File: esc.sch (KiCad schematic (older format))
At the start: 67 parts, among them IC1 4N25, IC2 LM25101, IC3 LM25101, IC4 LM25101, IC5 ATMEGA8-AI, P1 CONN_01X03, P2 CONN_01X03, P3 CONN_01X02, P4 CONN_02X02, P5 CONN_01X01, P6 CONN_01X01, Q1 MOSFET_N, Q10 MOSFET_N, Q11 MOSFET_N, Q12 MOSFET_N, Q2 MOSFET_N, Q3 MOSFET_N, Q4 MOSFET_N, Q5 MOSFET_N, Q6 MOSFET_N, Q7 MOSFET_N, Q8 MOSFET_N, Q9 MOSFET_N, U1 MCP1804, U2 LM2940 10V, Y1 RESONATEUR

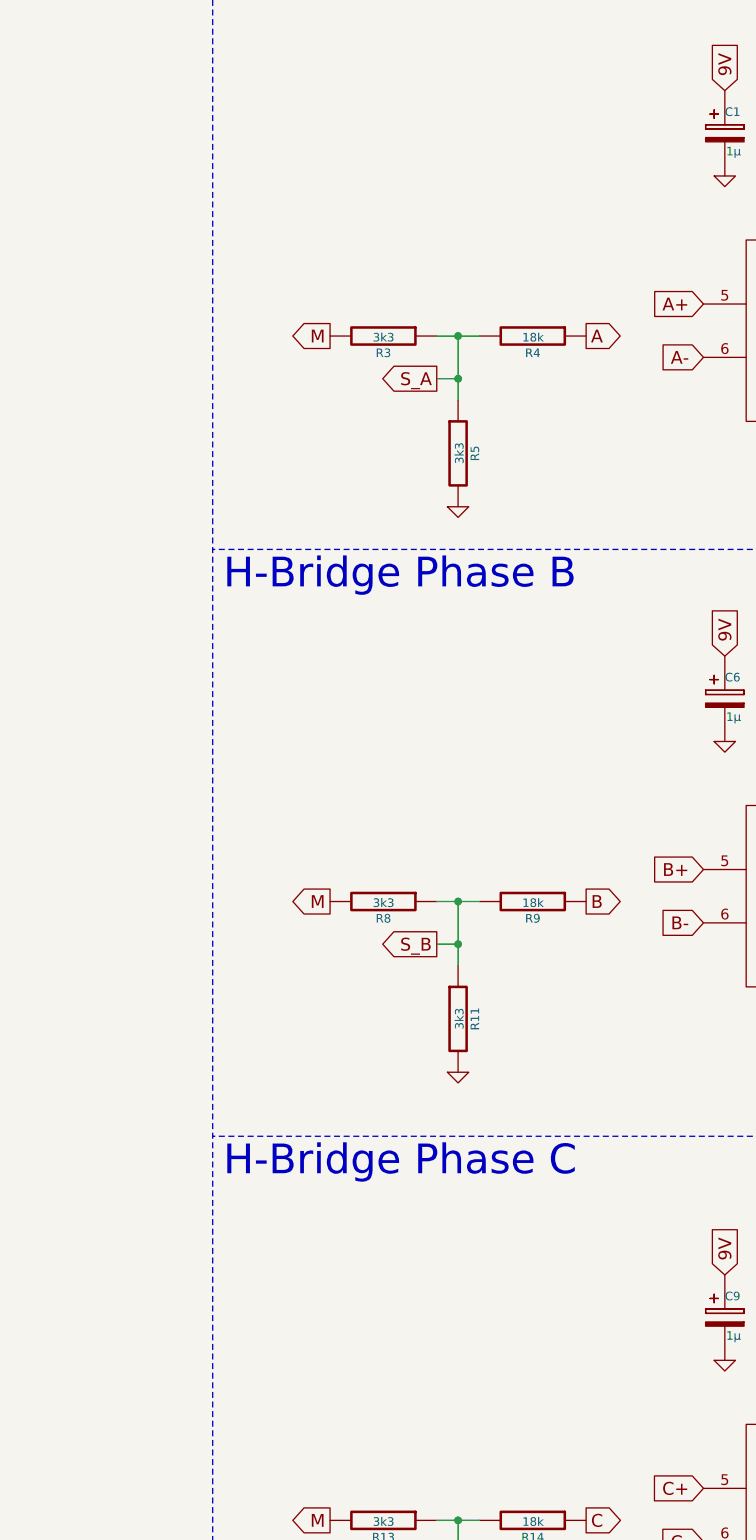
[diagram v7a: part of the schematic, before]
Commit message: Added pull down Resistors
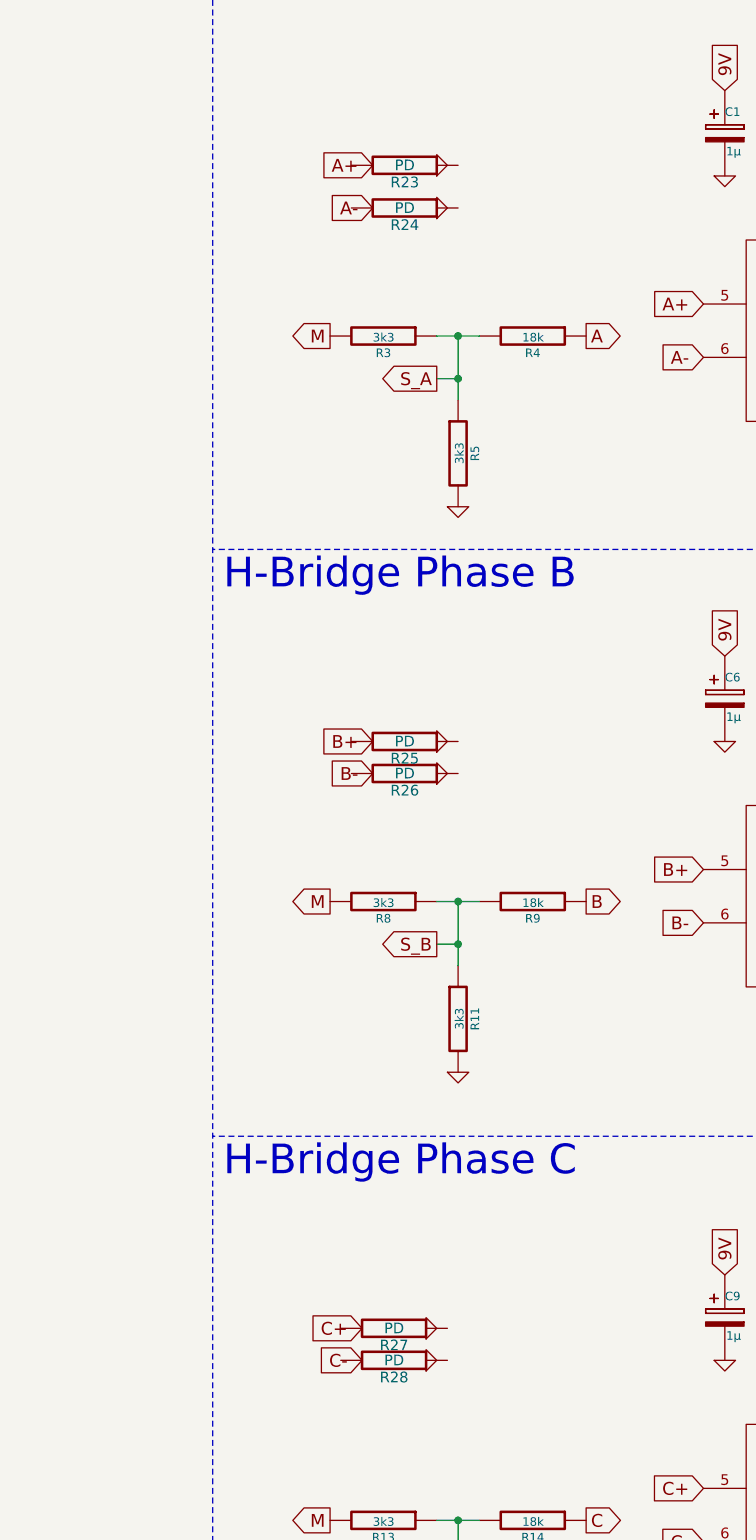
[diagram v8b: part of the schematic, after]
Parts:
- added R23, R24, R25, R26, R27, R28: PD, Resistors_SMD:R_0603_HandSoldering, symbol R
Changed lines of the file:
@@
 	1    0    0    -1
 $EndComp
+Text GLabel 9900 7350 0    60   Input ~ 0
+C+
+Text GLabel 9900 7500 0    60   Input ~ 0
+C-
+$Comp
+L R R27
+U 1 1 564C95B9
+P 10050 7350
+F 0 "R27" V 10130 7350 50  0000 C CNN
+F 1 "PD" V 10050 7350 50  0000 C CNN
+F 2 "Resistors_SMD:R_0603_HandSoldering" V 9980 7350 30  0001 C CNN
+F 3 "" H 10050 7350 30  0000 C CNN
+	1    10050 7350
+	0    1    1    0
+$EndComp
+$Comp
+L R R28
+U 1 1 564C9864
+P 10050 7500
+F 0 "R28" V 10130 7500 50  0000 C CNN
+F 1 "PD" V 10050 7500 50  0000 C CNN
+F 2 "Resistors_SMD:R_0603_HandSoldering" V 9980 7500 30  0001 C CNN
+F 3 "" H 10050 7500 30  0000 C CNN
+	1    10050 7500
+	0    1    1    0
+$EndComp
+$Comp
+L GND-RESCUE-esc #PWR049
+U 1 1 564C9D54
+P 10200 7350
+F 0 "#PWR049" H 10200 7350 30  0001 C CNN
+F 1 "GND" H 10200 7280 30  0001 C CNN
+F 2 "" H 10200 7350 60  0000 C CNN
+F 3 "" H 10200 7350 60  0000 C CNN
+	1    10200 7350
+	0    -1   -1   0
+$EndComp
+$Comp
+L GND-RESCUE-esc #PWR050
+U 1 1 564C9E2E
+P 10200 7500
+F 0 "#PWR050" H 10200 7500 30  0001 C CNN
+F 1 "GND" H 10200 7430 30  0001 C CNN
+F 2 "" H 10200 7500 60  0000 C CNN
+F 3 "" H 10200 7500 60  0000 C CNN
+	1    10200 7500
+	0    -1   -1   0
+$EndComp
+Text GLabel 9950 4750 0    60   Input ~ 0
+B-
+Text GLabel 9950 4600 0    60   Input ~ 0
+B+
+$Comp
+L R R25
+U 1 1 564CA584
+P 10100 4600
+F 0 "R25" V 10180 4600 50  0000 C CNN
+F 1 "PD" V 10100 4600 50  0000 C CNN
+F 2 "Resistors_SMD:R_0603_HandSoldering" V 10030 4600 30  0001 C CNN
+F 3 "" H 10100 4600 30  0000 C CNN
+	1    10100 4600
+	0    1    1    0
+$EndComp
+$Comp
+L R R26
+U 1 1 564CA6CE
+P 10100 4750
+F 0 "R26" V 10180 4750 50  0000 C CNN
+F 1 "PD" V 10100 4750 50  0000 C CNN
+F 2 "Resistors_SMD:R_0603_HandSoldering" V 10030 4750 30  0001 C CNN
+F 3 "" H 10100 4750 30  0000 C CNN
+	1    10100 4750
+	0    1    1    0
+$EndComp
+$Comp
+L GND-RESCUE-esc #PWR051
+U 1 1 564CA7B9
+P 10250 4600
+F 0 "#PWR051" H 10250 4600 30  0001 C CNN
+F 1 "GND" H 10250 4530 30  0001 C CNN
+F 2 "" H 10250 4600 60  0000 C CNN
+F 3 "" H 10250 4600 60  0000 C CNN
+	1    10250 4600
+	0    -1   -1   0
+$EndComp
+$Comp
+L GND-RESCUE-esc #PWR052
+U 1 1 564CA899
+P 10250 4750
+F 0 "#PWR052" H 10250 4750 30  0001 C CNN
+F 1 "GND" H 10250 4680 30  0001 C CNN
+F 2 "" H 10250 4750 60  0000 C CNN
+F 3 "" H 10250 4750 60  0000 C CNN
+	1    10250 4750
+	0    -1   -1   0
+$EndComp
+Text GLabel 9950 2100 0    60   Input ~ 0
+A-
+Text GLabel 9950 1900 0    60   Input ~ 0
+A+
+$Comp
+L R R23
+U 1 1 564CAD18
+P 10100 1900
+F 0 "R23" V 10180 1900 50  0000 C CNN
+F 1 "PD" V 10100 1900 50  0000 C CNN
+F 2 "Resistors_SMD:R_0603_HandSoldering" V 10030 1900 30  0001 C CNN
+F 3 "" H 10100 1900 30  0000 C CNN
+	1    10100 1900
+	0    1    1    0
+$EndComp
+$Comp
+L R R24
+U 1 1 564CAE4E
+P 10100 2100
+F 0 "R24" V 10180 2100 50  0000 C CNN
+F 1 "PD" V 10100 2100 50  0000 C CNN
+F 2 "Resistors_SMD:R_0603_HandSoldering" V 10030 2100 30  0001 C CNN
+F 3 "" H 10100 2100 30  0000 C CNN
+	1    10100 2100
+	0    1    1    0
+$EndComp
+$Comp
+L GND-RESCUE-esc #PWR053
+U 1 1 564CAF3D
+P 10250 1900
+F 0 "#PWR053" H 10250 1900 30  0001 C CNN
+F 1 "GND" H 10250 1830 30  0001 C CNN
+F 2 "" H 10250 1900 60  0000 C CNN
+F 3 "" H 10250 1900 60  0000 C CNN
+	1    10250 1900
+	0    -1   -1   0
+$EndComp
+$Comp
+L GND-RESCUE-esc #PWR054
+U 1 1 564CB023
+P 10250 2100
+F 0 "#PWR054" H 10250 2100 30  0001 C CNN
+F 1 "GND" H 10250 2030 30  0001 C CNN
+F 2 "" H 10250 2100 60  0000 C CNN
+F 3 "" H 10250 2100 60  0000 C CNN
+	1    10250 2100
+	0    -1   -1   0
+$EndComp
 $EndSCHEMATC
